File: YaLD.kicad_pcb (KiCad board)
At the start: 2 copper layers, 89 parts, among them IC1 ATMEGA32-A, IC2 PCA9685, IC3 PCA9685, J1 RJ45, J2 RJ45, K1 CONN_3, K2 DMXin, K3 DMXout, P1 CONN_2, P10 CONN_01X04, P11 CONN_01X04, P12 CONN_01X04, P13 CONN_01X04, P14 CONN_01X02, P2 ISP, P3 CONN_01X02, P4 CONN_01X04, P5 CONN_01X04, P6 CONN_01X04, P7 CONN_01X04, P8 CONN_01X04, P9 CONN_01X04, SW1 DIPS_10, U1 75LBC176, U10 IRF7103, U11 IRF7103, U12 IRF7103, U13 IRF7103, U14 IRF7103, U15 IRF7103, U16 IRF7103, U17 IRF7103, U18 IRF7103, U2 7805_f, U3 IRF7103, U4 IRF7103, U5 IRF7103, U6 IRF7103, U7 IRF7103, U8 IRF7103, U9 IRF7103, X1 16MHz

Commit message: fixed RJ45 connectors + folder libs.pretty added
RJ45 were on wrong side;
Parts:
- added P15: CONN_01X01, Socket_Strips:Socket_Strip_Straight_1x01, F.Cu at (57.3, 79.6)
- added P16: CONN_01X01, Socket_Strips:Socket_Strip_Straight_1x01, F.Cu at (63.7, 80.6)
- J1: value RJ45 -> RJDMXin; moved to B.Cu
- J2: value RJ45 -> RJDMXout; moved to B.Cu
- K1: value CONN_3 -> IR_RCV
- P1: value CONN_2 -> PWR_IN
- P2: footprint Pin_Headers:Pin_Header_Straight_2x05 -> 2x5smd:Pin_HeadersPin_Header_SMD_2x5; moved to B.Cu
- moved R3 28.2 mm to (60.5, 73.4), turned to 270 degrees
- moved P2 13.8 mm to (46.7, 38.3), turned to 270 degrees
- moved C2 12.3 mm to (54.7, 52.3), turned to 270 degrees
- moved C1 9.28 mm to (54.7, 57.6), turned to 270 degrees
- moved X1 4.96 mm to (49.8, 56.9)
- moved K1 3.36 mm to (59.4, 66.0), turned to 90 degrees
- moved C3 2.75 mm to (60.9, 57.1)
- moved R13 0.85 mm to (84.5, 64.8)
- moved R23 0.66 mm to (84.5, 56.1)
- moved C6 0.55 mm to (49.5, 85.3), turned to 180 degrees
- moved R22 0.50 mm to (84.5, 59.1)
- moved R12 0.27 mm to (84.5, 67.4)
- moved R24 0.27 mm to (84.6, 53.1)
- moved R25 0.19 mm to (84.5, 50.2)
- turned J1 to 90 degrees
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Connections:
- IC1 pad 14: Net-(IC1-Pad14) -> GND
- J1 pad 1: DMXminus -> DMXplus
- J1 pad 2: DMXplus -> DMXminus
- J1 pad 3: GND -> Net-(J1-Pad3)
- J1 pad 6: GND -> Net-(J1-Pad6)
- J1 pad 7: Net-(J1-Pad7) -> GND
- J1 pad 8: Net-(J1-Pad8) -> GND
- J2 pad 1: DMXminus -> DMXplus
- J2 pad 2: DMXplus -> DMXminus
- J2 pad 3: GND -> Net-(J2-Pad3)
- J2 pad 6: GND -> Net-(J2-Pad6)
- J2 pad 7: Net-(J2-Pad7) -> GND
- J2 pad 8: Net-(J2-Pad8) -> GND
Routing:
- net VCC: track 85.5 -> 267.7 mm
- net GND: track 8.90 -> 49.5 mm
- net RESET: track 0.00 -> 37.8 mm
- net DMXplus: track 47.2 -> 80.2 mm
- net MOSI: track 13.1 -> 38.2 mm
- net SCK: track 22.1 -> 36.2 mm
- net MISO: track 35.3 -> 29.3 mm
- net Net-(C3-Pad1): track 22.7 -> 27.7 mm
- net INT1: track 12.7 -> 7.88 mm
- net SCL: track 139.8 -> 143.2 mm
- net SDA: track 140.5 -> 143.2 mm
- net DMXminus: track 59.5 -> 57.1 mm
- net Net-(C2-Pad2): track 27.9 -> 25.8 mm
- net INT0: track 30.5 -> 31.8 mm
- net Net-(C1-Pad2): track 13.1 -> 14.4 mm
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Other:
- net class VCC_small added: clearance 0.254, trace_width 0.254, via_dia 0.889, via_drill 0.635

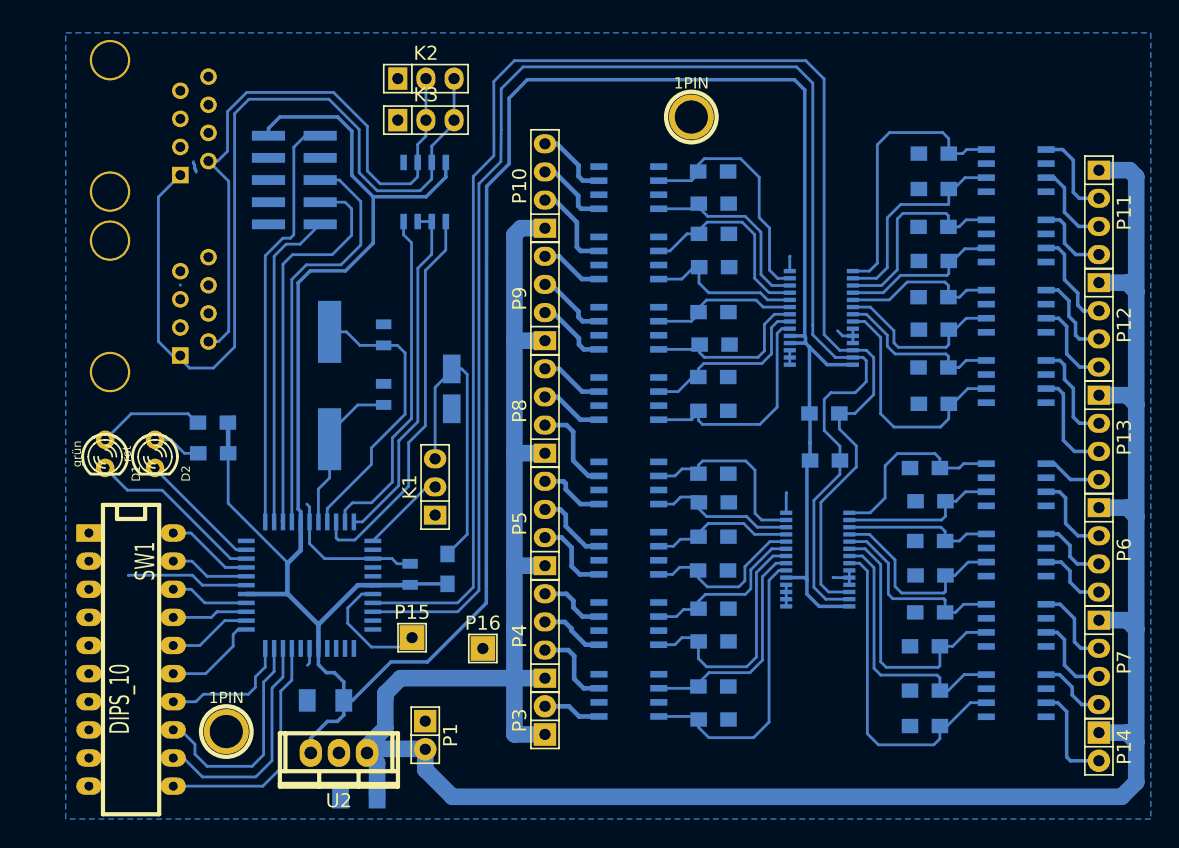
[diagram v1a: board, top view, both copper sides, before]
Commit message: refixed RJ45 - they have been on CORRECT side before!
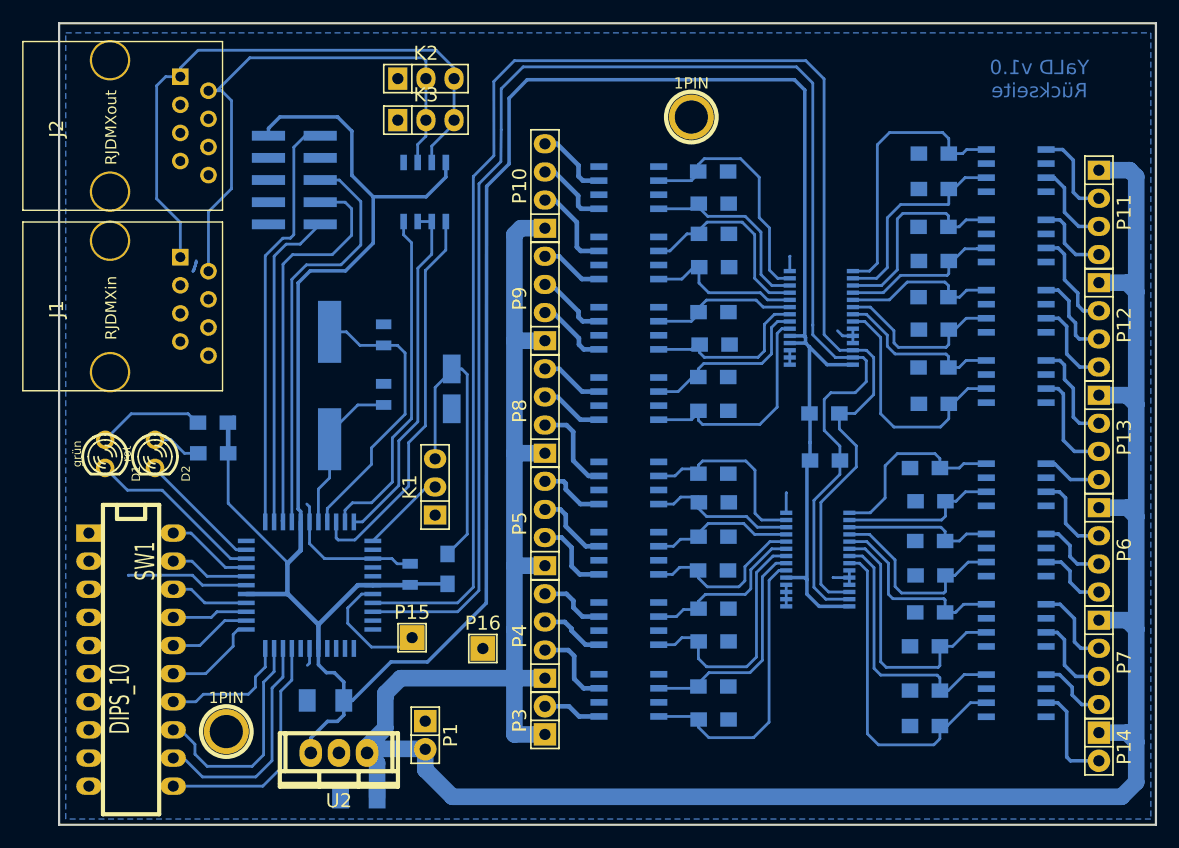
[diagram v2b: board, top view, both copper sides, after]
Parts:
- J1, J2: moved to F.Cu
- turned J1 to 270 degrees
- turned J2 to 270 degrees
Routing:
- net DMXplus: track 80.2 -> 55.0 mm
- net DMXminus: track 57.1 -> 49.2 mm
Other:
- board outline added: 99.1 x 72.4 mm
- board text added: "YaLD v1.0 Rückseite"

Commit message: DMX plus/minus switched, GND airwire connected
+ nicer silk print (more readable)
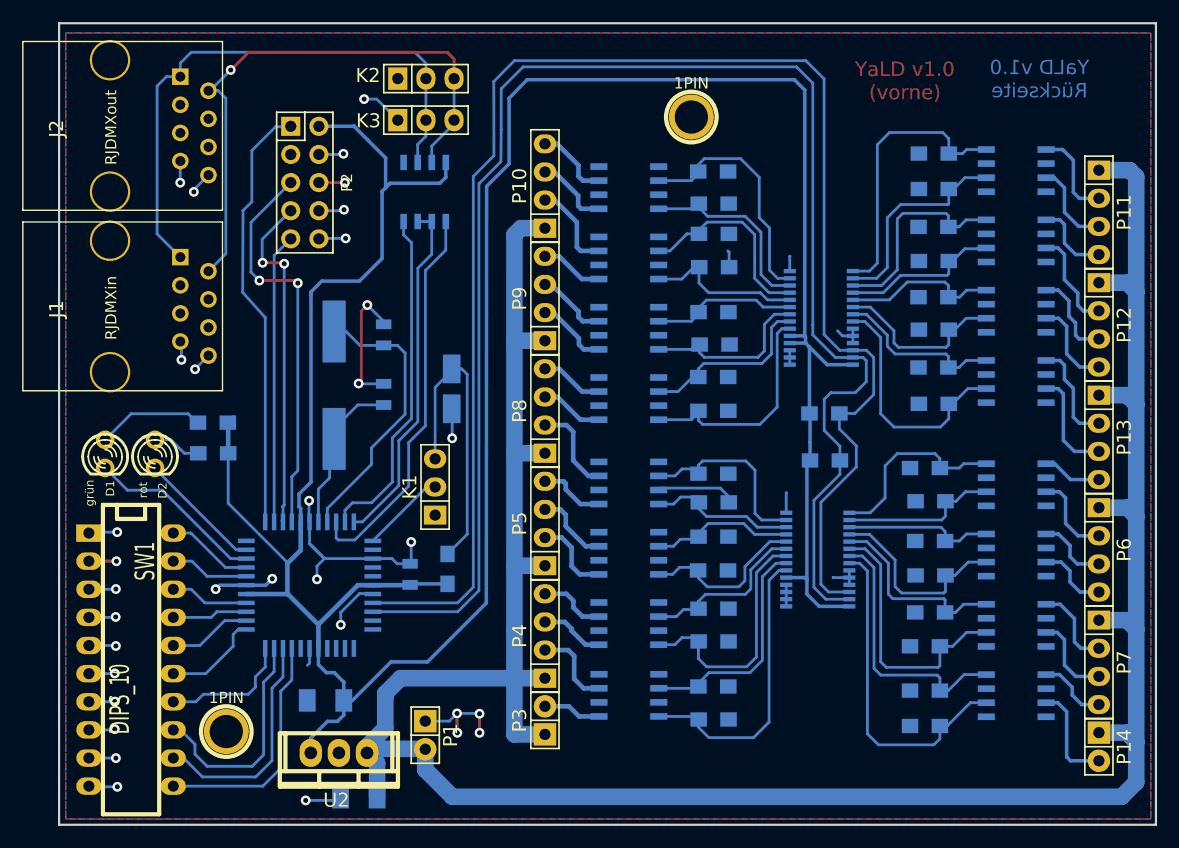
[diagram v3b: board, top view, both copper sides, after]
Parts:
- removed P15, P16: CONN_01X01, Socket_Strips:Socket_Strip_Straight_1x01
- P2: footprint 2x5smd:Pin_HeadersPin_Header_SMD_2x5 -> Pin_Headers:Pin_Header_Straight_2x05; moved to F.Cu
- moved P2 0.91 mm to (47.6, 38.5)
- moved X1 0.41 mm to (50.2, 56.8)
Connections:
- K2 pad 2: DMXminus -> DMXplus
- K2 pad 3: DMXplus -> DMXminus
- K3 pad 2: DMXminus -> DMXplus
- K3 pad 3: DMXplus -> DMXminus
- U1 pad 6: DMXminus -> DMXplus
- U1 pad 7: DMXplus -> DMXminus
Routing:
- net GND: track 49.5 -> 130.5 mm, vias 0 -> 33
- net VCC: track 267.7 -> 261.6 mm
- net SCK: track 36.2 -> 31.4 mm, vias 0 -> 2
- net DMXminus: track 49.2 -> 53.1 mm, vias 0 -> 1
- net MISO: track 29.3 -> 26.2 mm
- net DMXplus: track 55.0 -> 52.3 mm
- net RESET: track 37.8 -> 36.0 mm, vias 0 -> 2
- net (no net): track 1.08 -> 0.00 mm
- net MOSI: track 38.2 -> 39.1 mm
- added copper zone on F.Cu, net GND
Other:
- net class OUT_12V added: clearance 0.254, trace_width 0.5, via_dia 0.889, via_drill 0.635
- board text added: "YaLD v1.0 (vorne)"
